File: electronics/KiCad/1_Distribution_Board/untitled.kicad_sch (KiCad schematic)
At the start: 5 parts, among them J20 Conn_01x02, J21 Conn_01x02

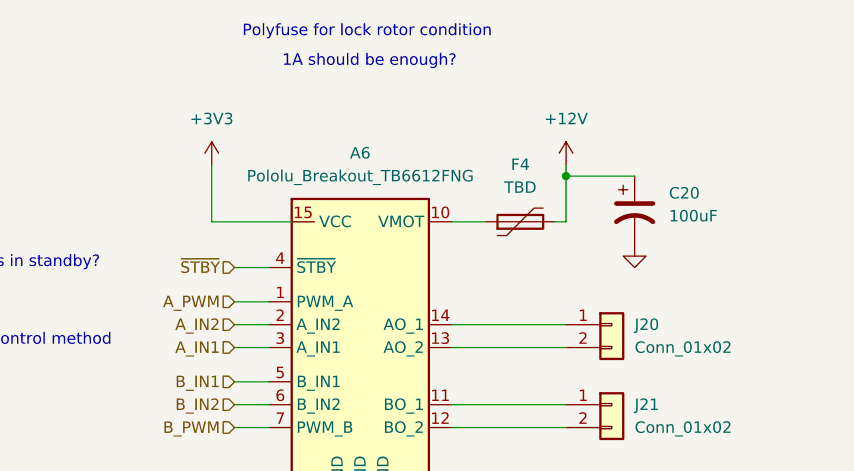
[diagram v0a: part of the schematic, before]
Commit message: footprint additions
Added Footprints to resistors and most components.
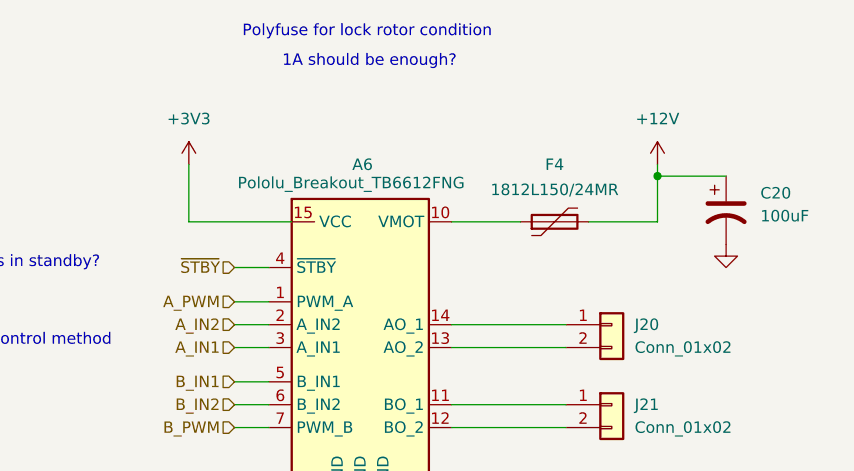
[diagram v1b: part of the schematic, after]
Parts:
- F4: value TBD -> 1812L150/24MR; footprint (none) -> Fuse:Fuse_1812_4532Metric_Pad1.30x3.40mm_HandSolder; JLCPCB Part # (none) -> C142805
- J20, J21: footprint (none) -> Connector_PinHeader_2.54mm:PinHeader_1x02_P2.54mm_Vertical
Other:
- moved on the sheet: C20, F4
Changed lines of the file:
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@@
 	)
 	(junction
-		(at 160.02 78.74)
+		(at 170.18 78.74)
 		(diameter 0)
 		(color 0 0 0 0)
@@
 	(wire
 		(pts
-			(xy 160.02 78.74) (xy 160.02 83.82)
+			(xy 170.18 78.74) (xy 170.18 83.82)
 		)
 		(stroke
@@
 	(wire
 		(pts
-			(xy 129.54 83.82) (xy 120.65 83.82)
+			(xy 129.54 83.82) (xy 118.11 83.82)
 		)
 		(stroke
@@
 	(wire
 		(pts
-			(xy 158.75 83.82) (xy 160.02 83.82)
+			(xy 123.19 95.25) (xy 127 95.25)
 		)
 		(stroke
@@
 	(wire
 		(pts
-			(xy 123.19 95.25) (xy 127 95.25)
+			(xy 123.19 106.68) (xy 127 106.68)
 		)
 		(stroke
@@
 	(wire
 		(pts
-			(xy 123.19 106.68) (xy 127 106.68)
+			(xy 160.02 106.68) (xy 147.32 106.68)
 		)
 		(stroke
@@
 	(wire
 		(pts
-			(xy 160.02 106.68) (xy 147.32 106.68)
+			(xy 134.62 116.84) (xy 134.62 120.65)
 		)
 		(stroke
@@
 	(wire
 		(pts
-			(xy 134.62 116.84) (xy 134.62 120.65)
+			(xy 160.02 95.25) (xy 147.32 95.25)
 		)
 		(stroke
@@
 	(wire
 		(pts
-			(xy 160.02 95.25) (xy 147.32 95.25)
+			(xy 170.18 78.74) (xy 177.8 78.74)
 		)
 		(stroke
@@
 	(wire
 		(pts
-			(xy 160.02 78.74) (xy 167.64 78.74)
+			(xy 123.19 101.6) (xy 127 101.6)
 		)
 		(stroke
@@
 	(wire
 		(pts
-			(xy 123.19 101.6) (xy 127 101.6)
+			(xy 162.56 83.82) (xy 170.18 83.82)
 		)
 		(stroke
@@
 	(wire
 		(pts
-			(xy 160.02 77.47) (xy 160.02 78.74)
+			(xy 170.18 77.47) (xy 170.18 78.74)
 		)
 		(stroke
@@
 	(wire
 		(pts
-			(xy 120.65 77.47) (xy 120.65 83.82)
+			(xy 118.11 77.47) (xy 118.11 83.82)
 		)
 		(stroke
@@
 	(wire
 		(pts
-			(xy 147.32 83.82) (xy 151.13 83.82)
+			(xy 147.32 83.82) (xy 154.94 83.82)
 		)
 		(stroke
@@
 			)
 		)
-		(property "Footprint" ""
+		(property "Footprint" "Connector_PinHeader_2.54mm:PinHeader_1x02_P2.54mm_Vertical"
 			(at 165.1 95.25 0)
 			(effects
@@
 		(on_board yes)
 		(dnp no)
-		(fields_autoplaced yes)
 		(property "Reference" "A6"
-			(at 137.16 76.2 0)
+			(at 137.414 77.47 0)
 			(effects
 				(font
@@
 		)
 		(property "Value" "Pololu_Breakout_TB6612FNG"
-			(at 137.16 78.74 0)
+			(at 136.144 79.502 0)
 			(effects
 				(font
@@
 	(symbol
 		(lib_id "power:+3V3")
-		(at 120.65 77.47 0)
+		(at 118.11 77.47 0)
 		(unit 1)
 		(exclude_from_sim no)
@@
 		(fields_autoplaced yes)
 		(property "Reference" "#PWR068"
-			(at 120.65 81.28 0)
+			(at 118.11 81.28 0)
 			(effects
 				(font
@@
 		)
 		(property "Value" "+3V3"
-			(at 120.65 72.39 0)
+			(at 118.11 72.39 0)
 			(effects
 				(font
@@
 		)
 		(property "Footprint" ""
-			(at 120.65 77.47 0)
+			(at 118.11 77.47 0)
 			(effects
 				(font
@@
 		)
 		(property "Datasheet" ""
-			(at 120.65 77.47 0)
+			(at 118.11 77.47 0)
 			(effects
 				(font
@@
 		)
 		(property "Description" "Power symbol creates a global label with name \"+3V3\""
-			(at 120.65 77.47 0)
+			(at 118.11 77.47 0)
 			(effects
 				(font
@@
 	(symbol
 		(lib_id "power:+12V")
-		(at 160.02 77.47 0)
+		(at 170.18 77.47 0)
 		(unit 1)
 		(exclude_from_sim no)
@@
 		(fields_autoplaced yes)
 		(property "Reference" "#PWR071"
-			(at 160.02 81.28 0)
+			(at 170.18 81.28 0)
 			(effects
 				(font
@@
 		)
 		(property "Value" "+12V"
-			(at 160.02 72.39 0)
+			(at 170.18 72.39 0)
 			(effects
 				(font
@@
 		)
 		(property "Footprint" ""
-			(at 160.02 77.47 0)
+			(at 170.18 77.47 0)
 			(effects
 				(font
@@
 		)
 		(property "Datasheet" ""
-			(at 160.02 77.47 0)
+			(at 170.18 77.47 0)
 			(effects
 				(font
@@
 		)
 		(property "Description" "Power symbol creates a global label with name \"+12V\""
-			(at 160.02 77.47 0)
+			(at 170.18 77.47 0)
 			(effects
 				(font
@@
 	(symbol
 		(lib_id "Device:C_Polarized_US")
-		(at 167.64 82.55 0)
+		(at 177.8 82.55 0)
 		(unit 1)
 		(exclude_from_sim no)
@@
 		(fields_autoplaced yes)
 		(property "Reference" "C20"
-			(at 171.45 80.6449 0)
+			(at 181.61 80.6449 0)
 			(effects
 				(font
@@
 		)
 		(property "Value" "100uF"
-			(at 171.45 83.1849 0)
+			(at 181.61 83.1849 0)
 			(effects
 				(font
@@
 		)
 		(property "Footprint" "Capacitor_THT:CP_Radial_D8.0mm_P2.50mm"
-			(at 167.64 82.55 0)
+			(at 177.8 82.55 0)
 			(effects
 				(font
@@
 		)
 		(property "Datasheet" "~"
-			(at 167.64 82.55 0)
+			(at 177.8 82.55 0)
 			(effects
 				(font
@@
 		)
 		(property "Description" "Polarized capacitor, US symbol"
-			(at 167.64 82.55 0)
+			(at 177.8 82.55 0)
 			(effects
 				(font
@@
 			)
 		)
-		(property "Footprint" ""
+		(property "Footprint" "Connector_PinHeader_2.54mm:PinHeader_1x02_P2.54mm_Vertical"
 			(at 165.1 104.14 0)
 			(effects
@@
 	(symbol
 		(lib_id "Device:Polyfuse")
-		(at 154.94 83.82 90)
+		(at 158.75 83.82 90)
 		(unit 1)
 		(exclude_from_sim no)
@@
 		(on_board yes)
 		(dnp no)
-		(fields_autoplaced yes)
 		(property "Reference" "F4"
-			(at 154.94 77.47 90)
+			(at 158.75 77.47 90)
 			(effects
 				(font
@@
 			)
 		)
-		(property "Value" "TBD"
-			(at 154.94 80.01 90)
+		(property "Value" "1812L150/24MR"
+			(at 158.75 80.264 90)
 			(effects
 				(font
@@
 			)
 		)
-		(property "Footprint" ""
-			(at 160.02 82.55 0)
+		(property "Footprint" "Fuse:Fuse_1812_4532Metric_Pad1.30x3.40mm_HandSolder"
+			(at 163.83 82.55 0)
 			(effects
 				(font
@@
 			)
 		)
-		(property "Datasheet" "~"
-			(at 154.94 83.82 0)
+		(property "Datasheet" "https://jlcpcb.com/api/file/downloadByFileSystemAccessId/8588941741143019520"
+			(at 158.75 83.82 0)
 			(effects
 				(font
@@
 		)
 		(property "Description" "Resettable fuse, polymeric positive temperature coefficient"
-			(at 154.94 83.82 0)
+			(at 158.75 83.82 0)
+			(effects
+				(font
+					(size 1.27 1.27)
+				)
+				(hide yes)
+			)
+		)
+		(property "JLCPCB Part #" "C142805"
+			(at 158.75 83.82 90)
 			(effects
 				(font
@@
 	(symbol
 		(lib_id "power:GND")
-		(at 167.64 86.36 0)
+		(at 177.8 86.36 0)
 		(unit 1)
 		(exclude_from_sim no)
@@
 		(fields_autoplaced yes)
 		(property "Reference" "#PWR097"
-			(at 167.64 92.71 0)
+			(at 177.8 92.71 0)
 			(effects
 				(font
@@
 		)
 		(property "Value" "GND"
-			(at 167.64 91.44 0)
+			(at 177.8 91.44 0)
 			(effects
 				(font
@@
 		)
 		(property "Footprint" ""
-			(at 167.64 86.36 0)
+			(at 177.8 86.36 0)
 			(effects
 				(font
@@
 		)
 		(property "Datasheet" ""
-			(at 167.64 86.36 0)
+			(at 177.8 86.36 0)
 			(effects
 				(font
@@
 		)
 		(property "Description" "Power symbol creates a global label with name \"GND\" , ground"
-			(at 167.64 86.36 0)
+			(at 177.8 86.36 0)
 			(effects
 				(font

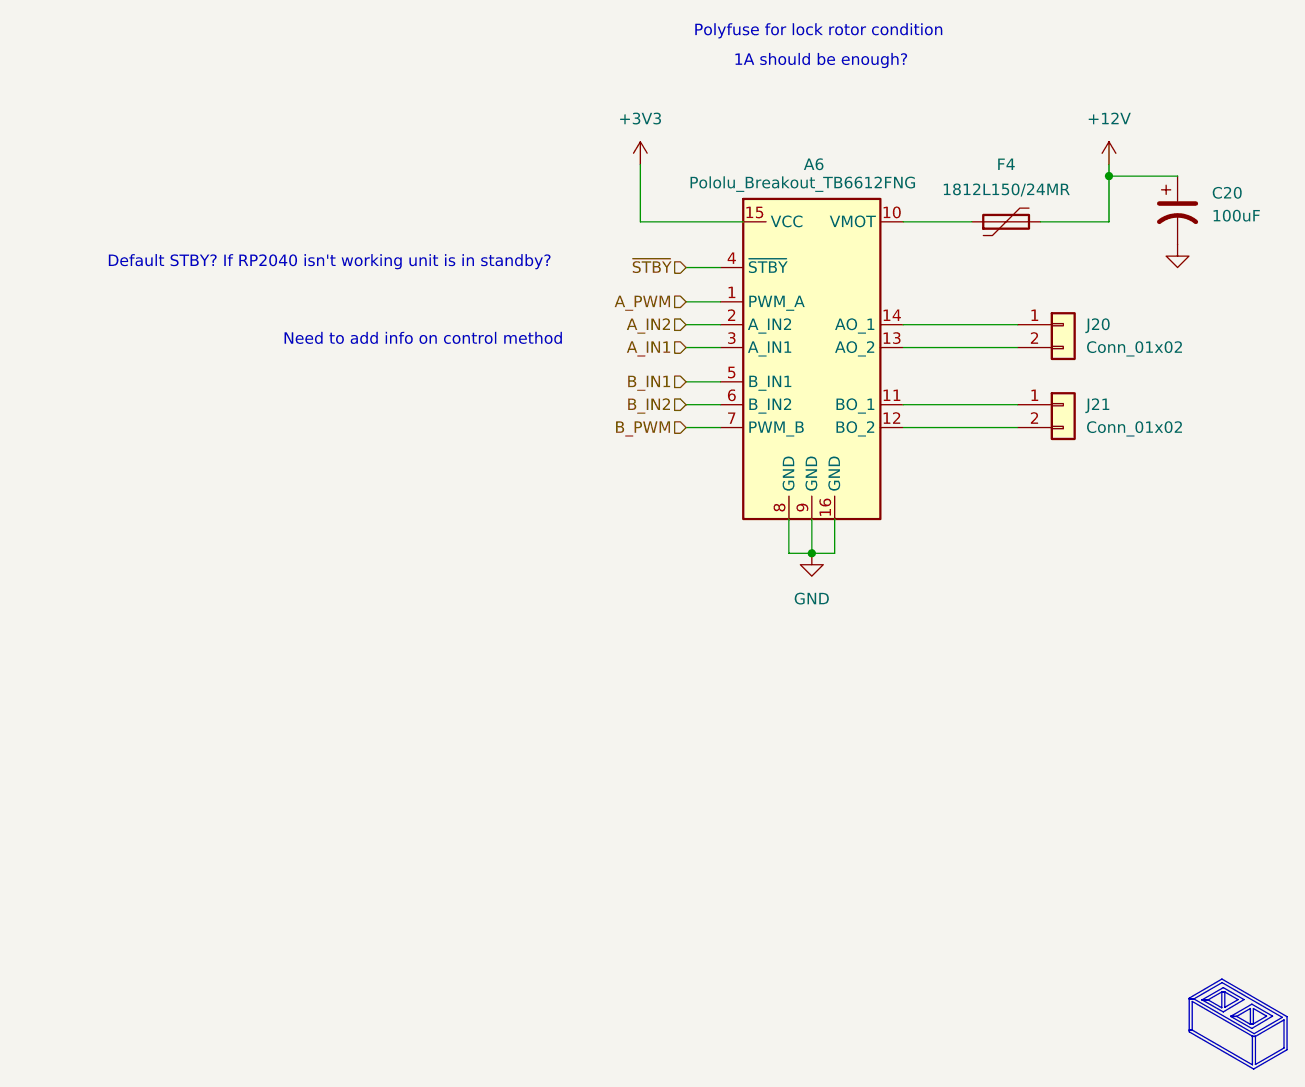
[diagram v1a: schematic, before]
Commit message: Updated to add 2 more steppers
Updated to add two more steppers, dual with the motor controllers. they will be either or. Layout hole pattern started. Still need some footprints assigned.
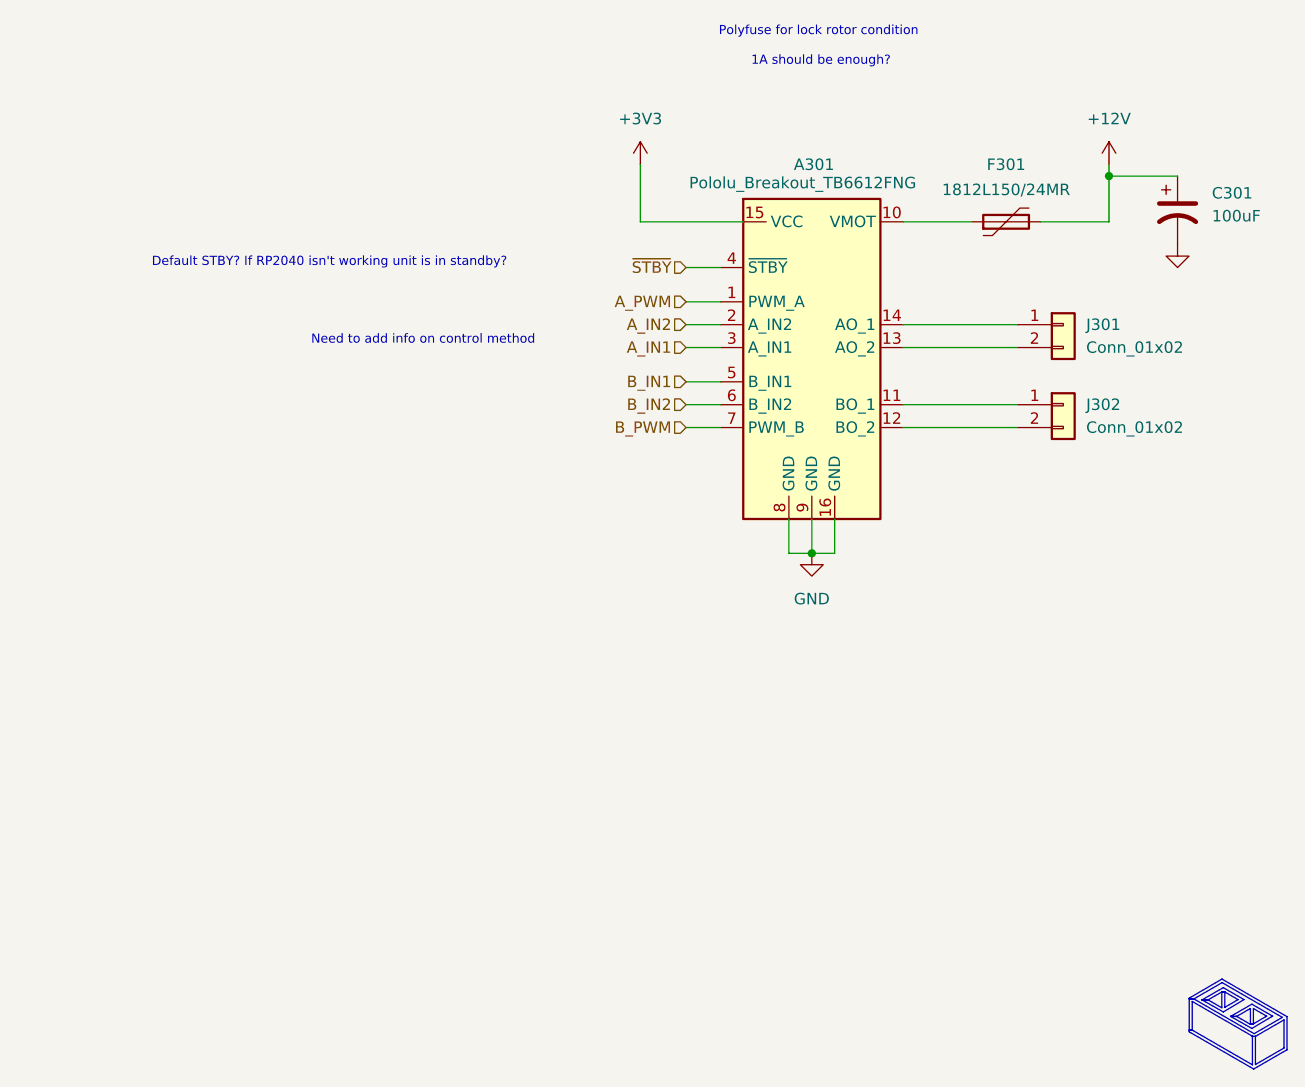
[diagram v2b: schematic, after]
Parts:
- renumbered A6 to A301, C20 to C301, F4 to F301, J20 to J301, J21 to J302
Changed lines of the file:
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@@
 		(effects
 			(font
-				(size 1.27 1.27)
+				(size 1.016 1.016)
 			)
 		)
@@
 		(effects
 			(font
-				(size 1.27 1.27)
+				(size 1.016 1.016)
 			)
 		)
@@
 		(effects
 			(font
-				(size 1.27 1.27)
+				(size 1.016 1.016)
 			)
 		)
@@
 		(effects
 			(font
-				(size 1.27 1.27)
+				(size 1.016 1.016)
 			)
 		)
@@
 		(dnp no)
 		(fields_autoplaced yes)
-		(property "Reference" "J20"
+		(property "Reference" "J301"
 			(at 167.64 95.2499 0)
 			(effects
@@
 			(project "1_Distribution_Board"
 				(path "/d53c8c01-e754-4310-8a73-7d7c95e64cd3/406ed9e9-c014-4ad1-b5c7-3c59cc994d52"
-					(reference "J4")
+					(reference "J401")
 					(unit 1)
 				)
 				(path "/d53c8c01-e754-4310-8a73-7d7c95e64cd3/6afb3c5f-c712-4230-bfac-30dcc87f4845"
-					(reference "J20")
+					(reference "J301")
 					(unit 1)
 				)
@@
 		(on_board yes)
 		(dnp no)
-		(property "Reference" "A6"
+		(property "Reference" "A301"
 			(at 137.414 77.47 0)
 			(effects
@@
 			(project "1_Distribution_Board"
 				(path "/d53c8c01-e754-4310-8a73-7d7c95e64cd3/406ed9e9-c014-4ad1-b5c7-3c59cc994d52"
-					(reference "A5")
+					(reference "A401")
 					(unit 1)
 				)
 				(path "/d53c8c01-e754-4310-8a73-7d7c95e64cd3/6afb3c5f-c712-4230-bfac-30dcc87f4845"
-					(reference "A6")
+					(reference "A301")
 					(unit 1)
 				)
@@
 		(dnp no)
 		(fields_autoplaced yes)
-		(property "Reference" "#PWR070"
+		(property "Reference" "#PWR0304"
 			(at 137.16 127 0)
 			(effects
@@
 			(project "1_Distribution_Board"
 				(path "/d53c8c01-e754-4310-8a73-7d7c95e64cd3/406ed9e9-c014-4ad1-b5c7-3c59cc994d52"
-					(reference "#PWR043")
+					(reference "#PWR0404")
 					(unit 1)
 				)
 				(path "/d53c8c01-e754-4310-8a73-7d7c95e64cd3/6afb3c5f-c712-4230-bfac-30dcc87f4845"
-					(reference "#PWR070")
+					(reference "#PWR0304")
 					(unit 1)
 				)
@@
 		(dnp no)
 		(fields_autoplaced yes)
-		(property "Reference" "#PWR068"
+		(property "Reference" "#PWR0301"
 			(at 118.11 81.28 0)
 			(effects
@@
 			(project "1_Distribution_Board"
 				(path "/d53c8c01-e754-4310-8a73-7d7c95e64cd3/406ed9e9-c014-4ad1-b5c7-3c59cc994d52"
-					(reference "#PWR042")
+					(reference "#PWR0401")
 					(unit 1)
 				)
 				(path "/d53c8c01-e754-4310-8a73-7d7c95e64cd3/6afb3c5f-c712-4230-bfac-30dcc87f4845"
-					(reference "#PWR068")
+					(reference "#PWR0301")
 					(unit 1)
 				)
@@
 		(dnp no)
 		(fields_autoplaced yes)
-		(property "Reference" "#PWR071"
+		(property "Reference" "#PWR0302"
 			(at 170.18 81.28 0)
 			(effects
@@
 			(project "1_Distribution_Board"
 				(path "/d53c8c01-e754-4310-8a73-7d7c95e64cd3/406ed9e9-c014-4ad1-b5c7-3c59cc994d52"
-					(reference "#PWR044")
+					(reference "#PWR0402")
 					(unit 1)
 				)
 				(path "/d53c8c01-e754-4310-8a73-7d7c95e64cd3/6afb3c5f-c712-4230-bfac-30dcc87f4845"
-					(reference "#PWR071")
+					(reference "#PWR0302")
 					(unit 1)
 				)
@@
 		(dnp no)
 		(fields_autoplaced yes)
-		(property "Reference" "C20"
+		(property "Reference" "C301"
 			(at 181.61 80.6449 0)
 			(effects
@@
 			(project "1_Distribution_Board"
 				(path "/d53c8c01-e754-4310-8a73-7d7c95e64cd3/406ed9e9-c014-4ad1-b5c7-3c59cc994d52"
-					(reference "C19")
+					(reference "C401")
 					(unit 1)
 				)
 				(path "/d53c8c01-e754-4310-8a73-7d7c95e64cd3/6afb3c5f-c712-4230-bfac-30dcc87f4845"
-					(reference "C20")
+					(reference "C301")
 					(unit 1)
 				)
@@
 		(dnp no)
 		(fields_autoplaced yes)
-		(property "Reference" "J21"
+		(property "Reference" "J302"
 			(at 167.64 104.1399 0)
 			(effects
@@
 			(project "1_Distribution_Board"
 				(path "/d53c8c01-e754-4310-8a73-7d7c95e64cd3/406ed9e9-c014-4ad1-b5c7-3c59cc994d52"
-					(reference "J13")
+					(reference "J402")
 					(unit 1)
 				)
 				(path "/d53c8c01-e754-4310-8a73-7d7c95e64cd3/6afb3c5f-c712-4230-bfac-30dcc87f4845"
-					(reference "J21")
+					(reference "J302")
 					(unit 1)
 				)
@@
 		(on_board yes)
 		(dnp no)
-		(property "Reference" "F4"
+		(property "Reference" "F301"
 			(at 158.75 77.47 90)
 			(effects
@@
 			(project "1_Distribution_Board"
 				(path "/d53c8c01-e754-4310-8a73-7d7c95e64cd3/406ed9e9-c014-4ad1-b5c7-3c59cc994d52"
-					(reference "F5")
+					(reference "F401")
 					(unit 1)
 				)
 				(path "/d53c8c01-e754-4310-8a73-7d7c95e64cd3/6afb3c5f-c712-4230-bfac-30dcc87f4845"
-					(reference "F4")
+					(reference "F301")
 					(unit 1)
 				)
@@
 		(dnp no)
 		(fields_autoplaced yes)
-		(property "Reference" "#PWR097"
+		(property "Reference" "#PWR0303"
 			(at 177.8 92.71 0)
 			(effects
@@
 			(project "1_Distribution_Board"
 				(path "/d53c8c01-e754-4310-8a73-7d7c95e64cd3/406ed9e9-c014-4ad1-b5c7-3c59cc994d52"
-					(reference "#PWR045")
+					(reference "#PWR0403")
 					(unit 1)
 				)
 				(path "/d53c8c01-e754-4310-8a73-7d7c95e64cd3/6afb3c5f-c712-4230-bfac-30dcc87f4845"
-					(reference "#PWR097")
+					(reference "#PWR0303")
 					(unit 1)
 				)
